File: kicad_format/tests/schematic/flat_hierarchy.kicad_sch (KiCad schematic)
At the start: 0 parts

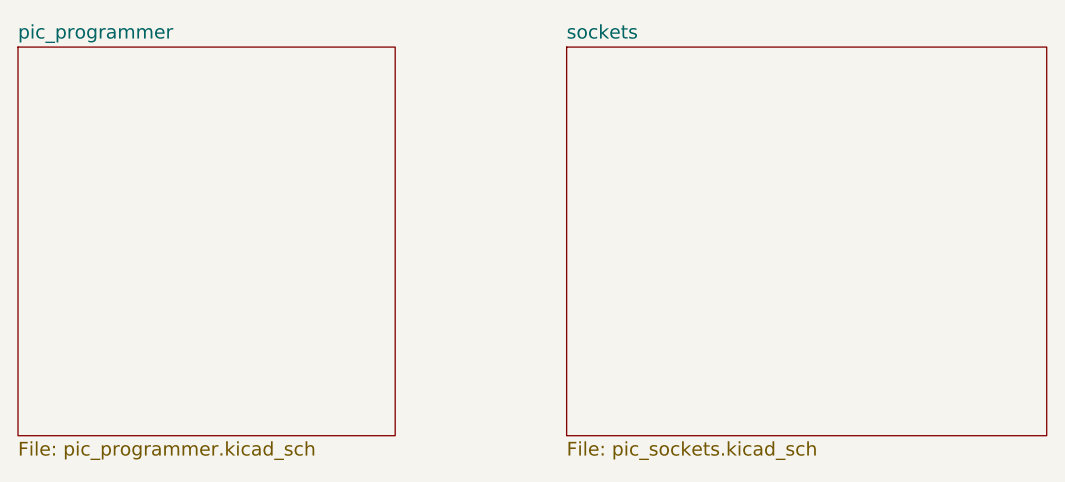
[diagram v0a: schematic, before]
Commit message: Add serialization context and support most modern kicad file idiosyncrasies
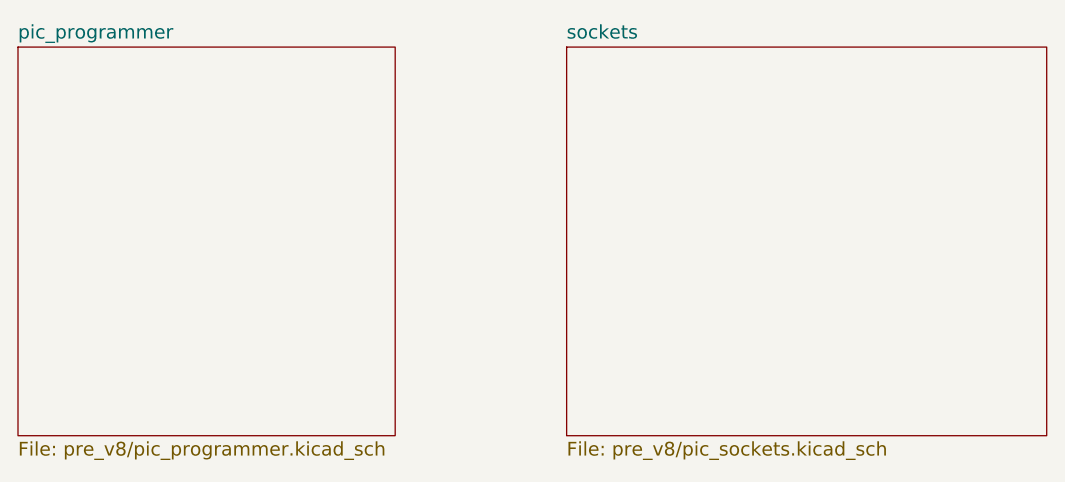
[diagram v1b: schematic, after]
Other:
- sheet pic_programmer: file pic_programmer.kicad_sch -> pre_v8/pic_programmer.kicad_sch
- sheet sockets: file pic_sockets.kicad_sch -> pre_v8/pic_sockets.kicad_sch
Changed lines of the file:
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@@
-(kicad_sch (version 20230121) (generator eeschema)
-  (paper "A4")
-  (title_block
-    (date "Sun 22 Mar 2015")
-    (rev "1")
-  )
-  (sheet (at 81.28 66.04) (size 41.91 43.18)
-    (stroke (width 0) (type solid))
-    (fill (color 0 0 0 0.0000))
-    (property "Sheetname" "pic_programmer" (at 81.28 65.2775 0)
-      (effects (font (size 1.524 1.524)) (justify left bottom))
-    )
-    (property "Sheetfile" "pic_programmer.kicad_sch" (at 81.28 109.8301 0)
-      (effects (font (size 1.524 1.524)) (justify left top))
-    )
-    (instances
-      (project "flat_hierarchy"
-        (path "/3bb135b1-15ed-43fe-a7bd-da79c3cfcb8b" (page "2"))
-      )
-    )
-  )
-  (sheet (at 142.24 66.04) (size 53.34 43.18)
-    (stroke (width 0) (type solid))
-    (fill (color 0 0 0 0.0000))
-    (property "Sheetname" "sockets" (at 142.24 65.2775 0)
-      (effects (font (size 1.524 1.524)) (justify left bottom))
-    )
-    (property "Sheetfile" "pic_sockets.kicad_sch" (at 142.24 109.8301 0)
-      (effects (font (size 1.524 1.524)) (justify left top))
-    )
-    (instances
-      (project "flat_hierarchy"
-        (path "/3bb135b1-15ed-43fe-a7bd-da79c3cfcb8b" (page "3"))
-      )
-    )
-  )
-  (sheet_instances
-    (path "/" (page "1"))
-  )
+(kicad_sch
+	(version 20250114)
+	(generator "eeschema")
+	(generator_version "9.0")
+	(paper "A4")
+	(title_block
+		(date "Sun 22 Mar 2015")
+		(rev "1")
+	)
+	(sheet
+		(at 81.28 66.04)
+		(size 41.91 43.18)
+		(exclude_from_sim no)
+		(in_bom yes)
+		(on_board yes)
+		(dnp no)
+		(stroke
+			(width 0)
+			(type solid)
+		)
+		(fill
+			(color 0 0 0 0.0000)
+		)
+		(property "Sheetname" "pic_programmer"
+			(at 81.28 65.2775 0)
+			(effects
+				(font
+					(size 1.524 1.524)
+				)
+				(justify left bottom)
+			)
+		)
+		(property "Sheetfile" "pre_v8/pic_programmer.kicad_sch"
+			(at 81.28 109.8301 0)
+			(effects
+				(font
+					(size 1.524 1.524)
+				)
+				(justify left top)
+			)
+		)
+		(instances
+			(project "flat_hierarchy"
+				(path "/3bb135b1-15ed-43fe-a7bd-da79c3cfcb8b"
+					(page "2")
+				)
+			)
+		)
+	)
+	(sheet
+		(at 142.24 66.04)
+		(size 53.34 43.18)
+		(exclude_from_sim no)
+		(in_bom yes)
+		(on_board yes)
+		(dnp no)
+		(stroke
+			(width 0)
+			(type solid)
+		)
+		(fill
+			(color 0 0 0 0.0000)
+		)
+		(property "Sheetname" "sockets"
+			(at 142.24 65.2775 0)
+			(effects
+				(font
+					(size 1.524 1.524)
+				)
+				(justify left bottom)
+			)
+		)
+		(property "Sheetfile" "pre_v8/pic_sockets.kicad_sch"
+			(at 142.24 109.8301 0)
+			(effects
+				(font
+					(size 1.524 1.524)
+				)
+				(justify left top)
+			)
+		)
+		(instances
+			(project "flat_hierarchy"
+				(path "/3bb135b1-15ed-43fe-a7bd-da79c3cfcb8b"
+					(page "3")
+				)
+			)
+		)
+	)
+	(sheet_instances
+		(path "/"
+			(page "1")
+		)
+	)
+	(embedded_fonts no)
 )
